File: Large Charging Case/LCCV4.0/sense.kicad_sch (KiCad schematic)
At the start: 8 parts, among them U18 XL2902-TS

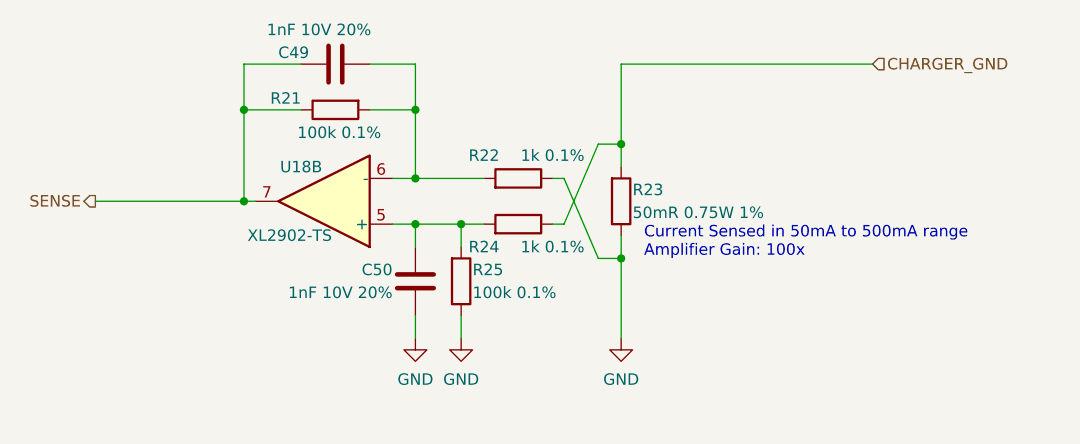
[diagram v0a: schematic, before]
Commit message: Super6, LCCV4 updates and Kicad8
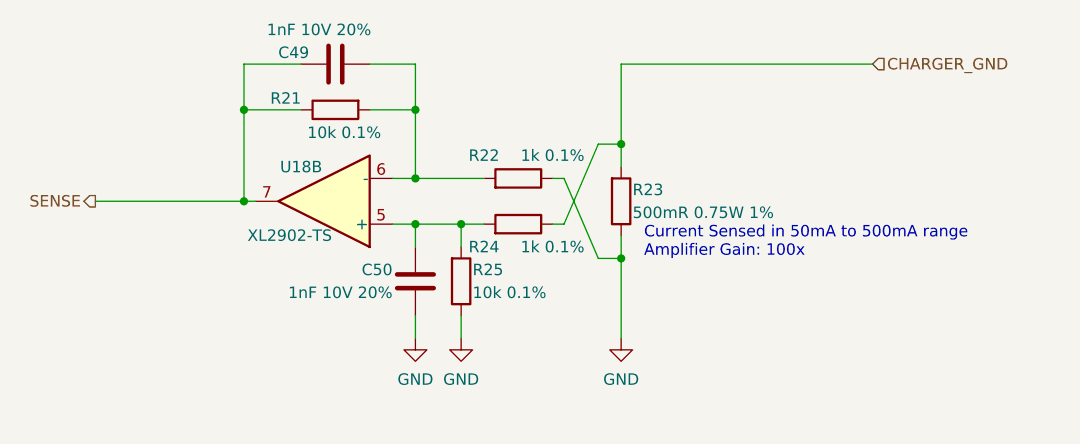
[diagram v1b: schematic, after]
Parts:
- R21, R25: value 100k 0.1% -> 10k 0.1%; LCSC Part Number (none) -> C2961361; Manufacturer Part Number TC02G1003BT -> TC02G1002BT
- R23: value 50mR 0.75W 1% -> 500mR 0.75W 1%; Manufacturer UNI-ROYAL(Uniroyal Elec) -> YAGEO; Manufacturer Part Number 201007F500MT4E -> RL2010FK-070R5L
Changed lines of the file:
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@@
       (effects (font (size 1.27 1.27)) (justify left))
     )
-    (property "Value" "100k 0.1%" (at 110.49 91.44 90)
+    (property "Value" "10k 0.1%" (at 110.49 91.44 90)
       (effects (font (size 1.27 1.27)) (justify left))
     )
@@
       (effects (font (size 1.27 1.27)) hide)
     )
-    (property "LCSC Part Number" "" (at 105.41 88.9 0)
+    (property "LCSC Part Number" "C2961361" (at 105.41 88.9 0)
       (effects (font (size 1.27 1.27)) hide)
     )
@@
       (effects (font (size 1.27 1.27)) hide)
     )
-    (property "Manufacturer Part Number" "TC02G1003BT" (at 105.41 88.9 0)
+    (property "Manufacturer Part Number" "TC02G1002BT" (at 105.41 88.9 0)
       (effects (font (size 1.27 1.27)) hide)
     )
@@
       (effects (font (size 1.27 1.27)) (justify left))
     )
-    (property "Value" "50mR 0.75W 1%" (at 138.43 100.33 0)
+    (property "Value" "500mR 0.75W 1%" (at 138.43 100.33 0)
       (effects (font (size 1.27 1.27)) (justify left))
     )
@@
       (effects (font (size 1.27 1.27)) hide)
     )
-    (property "Manufacturer" "UNI-ROYAL(Uniroyal Elec)" (at 137.16 99.06 0)
-      (effects (font (size 1.27 1.27)) hide)
-    )
-    (property "Manufacturer Part Number" "201007F500MT4E" (at 137.16 99.06 0)
+    (property "Manufacturer" "YAGEO" (at 137.16 99.06 0)
+      (effects (font (size 1.27 1.27)) hide)
+    )
+    (property "Manufacturer Part Number" "RL2010FK-070R5L" (at 137.16 99.06 0)
       (effects (font (size 1.27 1.27)) hide)
     )
@@
       (effects (font (size 1.27 1.27)) (justify left))
     )
-    (property "Value" "100k 0.1%" (at 120.65 109.22 0)
+    (property "Value" "10k 0.1%" (at 120.65 109.22 0)
       (effects (font (size 1.27 1.27)) (justify left))
     )
@@
       (effects (font (size 1.27 1.27)) hide)
     )
-    (property "LCSC Part Number" "" (at 119.38 107.95 0)
+    (property "LCSC Part Number" "C2961361" (at 119.38 107.95 0)
       (effects (font (size 1.27 1.27)) hide)
     )
@@
       (effects (font (size 1.27 1.27)) hide)
     )
-    (property "Manufacturer Part Number" "TC02G1003BT" (at 119.38 107.95 0)
-      (effects (font (size 1.27 1.27)) hide)
-    )
+    (property "Manufacturer Part Number" "TC02G1002BT" (at 119.38 107.95 0)
+      (effects (font (size 1.27 1.27)) hide)
+    )

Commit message: Updated a bunch of boards, added Jogs and 12mm D6 proto
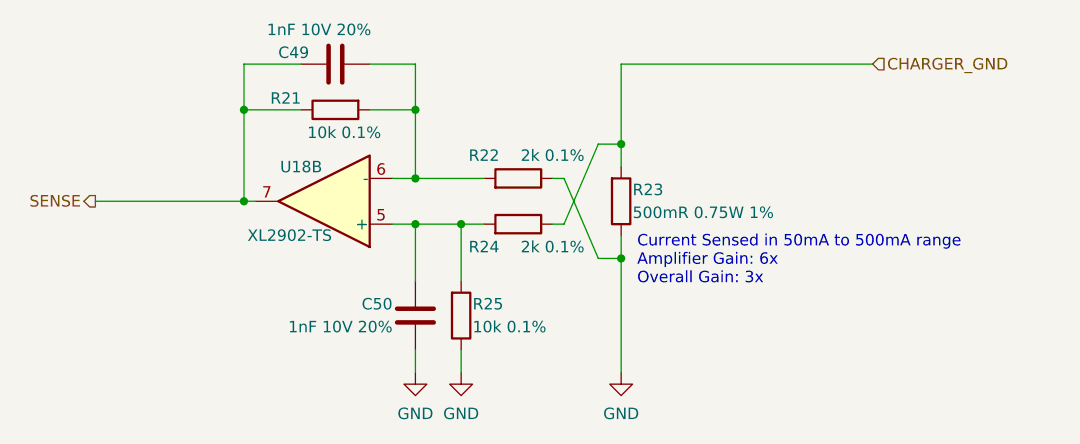
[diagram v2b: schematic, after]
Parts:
- R22, R24: value 1k 0.1% -> 2k 0.1%; Manufacturer Fenghua -> YAGEO; Manufacturer Part Number TC02G1001BT -> RT0402BRD072KL
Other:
- note added: "Current Sensed in 50mA to 500mA range Amplifier Gain: 6x Overall Gain: 3x"
- note removed: "Current Sensed in 50mA to 500mA range Amplifier Gain: 100x"
- moved on the sheet: C50, R25
